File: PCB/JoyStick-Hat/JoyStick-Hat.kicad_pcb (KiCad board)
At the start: 2 copper layers, 73 parts, among them J1 Conn_02x10_Counter_Clockwise, J10 Conn_01x02_Pin, J11 Conn_01x02_Pin, J12 BU2032SM-JJ-GTR, J13 20021121-00010C4LF, J14 0675031020, J2 Conn_02x10_Counter_Clockwise, J3 Raspberry_Pi_2_3, J4 Conn_01x03_Pin, J5 Conn_01x03_Pin, J6 Conn_01x04_Pin, J7 Conn_01x02_Pin, J8 Conn_01x02_Pin, J9 Conn_01x04_Pin, M1 D24V22F12, M2 D24V22F5, M3 D24V22F3, SW1 TL3301NF260QG, U2 TLC5947DAP, U3 TLC5947DAP, U4 MAX3535ECWI+T, U5 STM32F446VETx, X1 ABM3B-8.000MHZ-B2-T, X2 ABS07-32.768KHZ-9-T

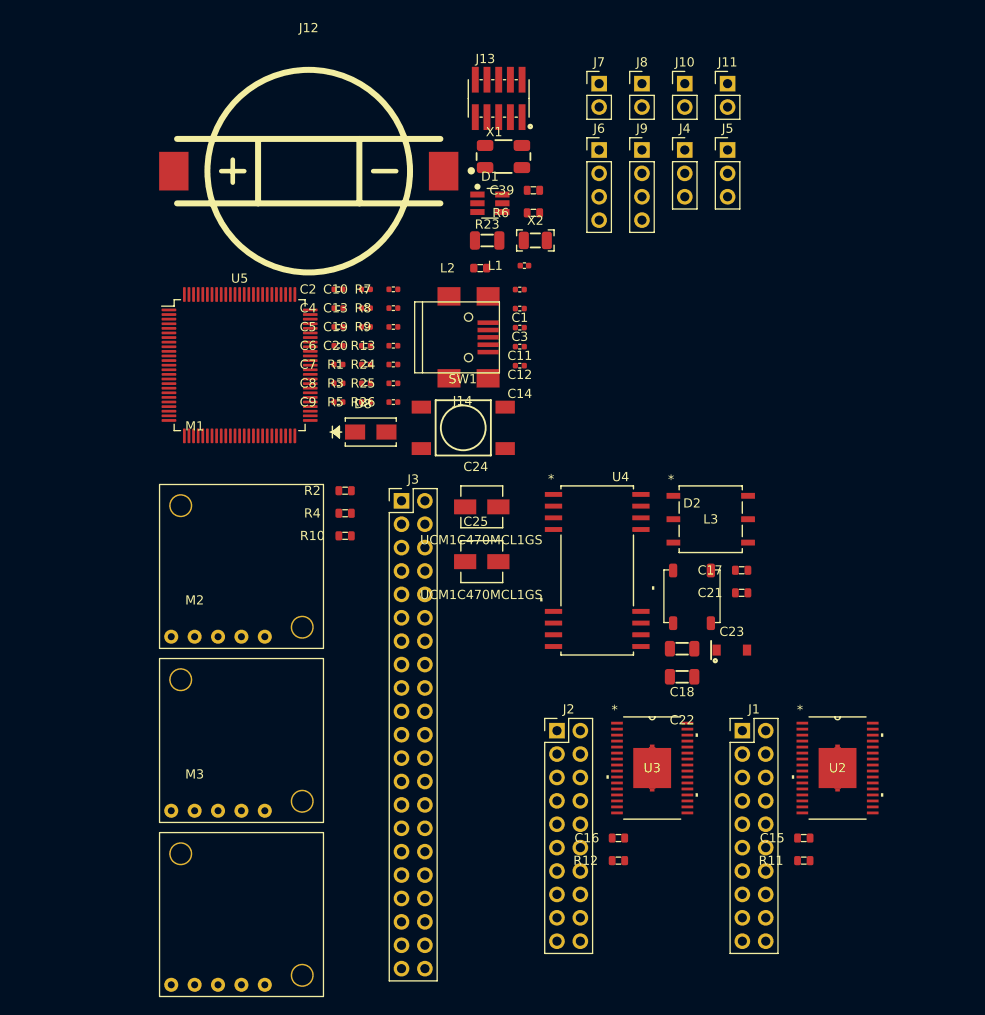
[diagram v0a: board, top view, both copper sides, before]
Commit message: LEDs and Additional connectors
Added heartbeat and diagnostic LEDs to STM32 and RPi3 schematics so we can directly flash them for debug purposes. Added a connector for serial port diagnostics on STM32. Added rotary switch interface for STM32 and added pullups to button connectors.
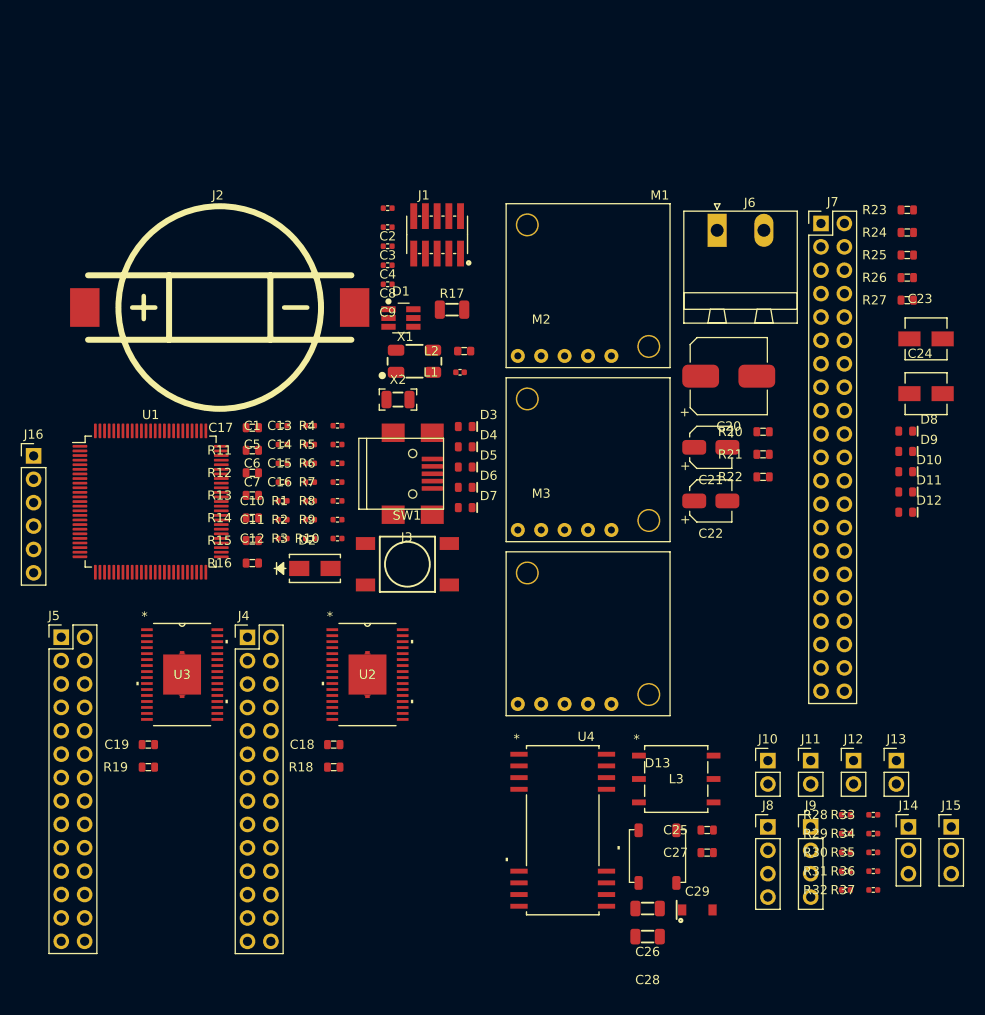
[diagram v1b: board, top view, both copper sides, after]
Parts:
- removed C39: C0603X103K1RAC3316, AVR-KiCAD-Lib-Capacitors:C0603
- removed U5: STM32F446VETx, Package_QFP:LQFP-100_14x14mm_P0.5mm
- added C26: CGA5L3X5R1V106K160AB, AVR-KiCAD-Lib-Capacitors:C1206, F.Cu at (155.7, 123.5)
- added C27: CL10B104JB8NNNC, AVR-KiCAD-Lib-Capacitors:C0603, F.Cu at (162.1, 117.4)
- added C28: CGA5L3X5R1V106K160AB, AVR-KiCAD-Lib-Capacitors:C1206, F.Cu at (155.7, 126.5)
- added C29: C1206C105K3RACAUTO, AVR-KiCAD-Lib-Diodes:D_SOD-123, F.Cu at (161.1, 123.6)
- added D10: LTST-C194KGKT, AVR-KiCAD-Lib-Diodes:LED0603, F.Cu at (183.7, 76.0)
- added D11: LTST-C194KGKT, AVR-KiCAD-Lib-Diodes:LED0603, F.Cu at (183.7, 78.2)
- added D12: LTST-C194KGKT, AVR-KiCAD-Lib-Diodes:LED0603, F.Cu at (183.7, 80.4)
- added D13: LMB110S-TP, AVR-KiCAD-Lib-Diodes:LMB110S-TP, F.Cu at (156.7, 117.8)
- added D3: LTST-C194TBKT, AVR-KiCAD-Lib-Diodes:LED0603, F.Cu at (135.9, 71.1)
- added D4: LTST-C194TBKT, AVR-KiCAD-Lib-Diodes:LED0603, F.Cu at (135.9, 73.3)
- added D5: LTST-C194TBKT, AVR-KiCAD-Lib-Diodes:LED0603, F.Cu at (135.9, 75.5)
- added D6: LTST-C194TBKT, AVR-KiCAD-Lib-Diodes:LED0603, F.Cu at (135.9, 77.7)
- added D7: LTST-C194TBKT, AVR-KiCAD-Lib-Diodes:LED0603, F.Cu at (135.9, 79.9)
- added D9: LTST-C194KGKT, AVR-KiCAD-Lib-Diodes:LED0603, F.Cu at (183.7, 73.8)
- added J15: Conn_01x03_Pin, Connector_PinHeader_2.54mm:PinHeader_1x03_P2.54mm_Vertical, F.Cu at (188.6, 114.6)
- added J16: Conn_01x06, Connector_PinHeader_2.54mm:PinHeader_1x06_P2.54mm_Vertical, F.Cu at (89.0, 74.3)
- added R14: RC0603FR-07470RL, AVR-KiCAD-Lib-Resistors:R0603, F.Cu at (112.8, 81.0)
- added R15: RC0603FR-07470RL, AVR-KiCAD-Lib-Resistors:R0603, F.Cu at (112.8, 83.5)
- added R16: RC0603FR-07470RL, AVR-KiCAD-Lib-Resistors:R0603, F.Cu at (112.8, 85.9)
- added R17: RC1206FR-071ML, AVR-KiCAD-Lib-Resistors:R1206, F.Cu at (134.4, 58.4)
- added R18: RMCF0603FT2K61, AVR-KiCAD-Lib-Resistors:R0603, F.Cu at (121.6, 108.1)
- added R19: RMCF0603FT2K61, AVR-KiCAD-Lib-Resistors:R0603, F.Cu at (101.5, 108.1)
- added R20: RC0603JR-07270RL, AVR-KiCAD-Lib-Resistors:R0603, F.Cu at (168.2, 71.7)
- added R21: RC0603JR-07270RL, AVR-KiCAD-Lib-Resistors:R0603, F.Cu at (168.2, 74.1)
- added R22: RC0603JR-07270RL, AVR-KiCAD-Lib-Resistors:R0603, F.Cu at (168.2, 76.6)
- added R27: RC0603FR-07470RL, AVR-KiCAD-Lib-Resistors:R0603, F.Cu at (183.9, 57.4)
- added R28: RC0402FR-071KL, AVR-KiCAD-Lib-Resistors:R0402, F.Cu at (177.2, 113.3)
- added R29: RC0402FR-071KL, AVR-KiCAD-Lib-Resistors:R0402, F.Cu at (177.2, 115.3)
- added R30: RC0402FR-071KL, AVR-KiCAD-Lib-Resistors:R0402, F.Cu at (177.2, 117.4)
- added R31: RC0402FR-071KL, AVR-KiCAD-Lib-Resistors:R0402, F.Cu at (177.2, 119.4)
- added R32: RC0402FR-071KL, AVR-KiCAD-Lib-Resistors:R0402, F.Cu at (177.2, 121.4)
- added R33: RC0402FR-071KL, AVR-KiCAD-Lib-Resistors:R0402, F.Cu at (180.2, 113.3)
- added R34: RC0402FR-071KL, AVR-KiCAD-Lib-Resistors:R0402, F.Cu at (180.2, 115.3)
- added R35: RC0402FR-071KL, AVR-KiCAD-Lib-Resistors:R0402, F.Cu at (180.2, 117.4)
- added R36: RC0402FR-071KL, AVR-KiCAD-Lib-Resistors:R0402, F.Cu at (180.2, 119.4)
- added R37: RC0402FR-071KL, AVR-KiCAD-Lib-Resistors:R0402, F.Cu at (180.2, 121.4)
- added U1: STM32F446VETx, Package_QFP:LQFP-100_14x14mm_P0.5mm, F.Cu at (101.7, 79.3)
- C1: value GCM1555C1H180GA16D -> C0402C104K9PACTU; footprint AVR-KiCAD-Lib-Capacitors:C0402 -> AVR-KiCAD-Lib-Resistors:R0402
- C11, C12: value CL05C090CB5NNNC -> C0402C104K9PACTU; footprint AVR-KiCAD-Lib-Capacitors:C0402 -> AVR-KiCAD-Lib-Resistors:R0402
- C14: value GRM155R60J475ME47D -> C0402C104K9PACTU; footprint AVR-KiCAD-Lib-Capacitors:C0402 -> AVR-KiCAD-Lib-Resistors:R0402
- C15, C16: value CL10B104JB8NNNC -> C0402C104K9PACTU; footprint AVR-KiCAD-Lib-Capacitors:C0603 -> AVR-KiCAD-Lib-Resistors:R0402
- C17: value CL10B104JB8NNNC -> C0603X103K1RAC3316
- C18: value CGA5L3X5R1V106K160AB -> CL10B104JB8NNNC; footprint AVR-KiCAD-Lib-Capacitors:C1206 -> AVR-KiCAD-Lib-Capacitors:C0603
- C19: value C0402C104K9PACTU -> CL10B104JB8NNNC; footprint AVR-KiCAD-Lib-Resistors:R0402 -> AVR-KiCAD-Lib-Capacitors:C0603
- C2, C4: value C0402C104K9PACTU -> GCM1555C1H180GA16D; footprint AVR-KiCAD-Lib-Resistors:R0402 -> AVR-KiCAD-Lib-Capacitors:C0402
- C20: value C0402C104K9PACTU -> UUQ1H470MCL1GS; footprint AVR-KiCAD-Lib-Resistors:R0402 -> AVR-KiCAD-Lib-Capacitors:CP_Elec_8x10
- C21: value CL10B104JB8NNNC -> UUQ1H100MCL1GB; footprint AVR-KiCAD-Lib-Capacitors:C0603 -> AVR-KiCAD-Lib-Capacitors:CP_Elec_4x5.3
- C22: value CGA5L3X5R1V106K160AB -> UUQ1H010MCL1GB; footprint AVR-KiCAD-Lib-Capacitors:C1206 -> AVR-KiCAD-Lib-Capacitors:CP_Elec_4x5.3
- C23: value C1206C105K3RACAUTO -> UCM1C470MCL1GS; footprint AVR-KiCAD-Lib-Diodes:D_SOD-123 -> AVR-KiCAD-Lib-Capacitors:UCM1C470MCL1GS
- C25: value UCM1C470MCL1GS -> CL10B104JB8NNNC; footprint AVR-KiCAD-Lib-Capacitors:UCM1C470MCL1GS -> AVR-KiCAD-Lib-Capacitors:C0603
- C3: value GCM1555C1H180GA16D -> GRM155R60J475ME47D
- C8, C9: value C0402C104K9PACTU -> CL05C090CB5NNNC; footprint AVR-KiCAD-Lib-Resistors:R0402 -> AVR-KiCAD-Lib-Capacitors:C0402
- D2: value LMB110S-TP -> SMAJ30CA; footprint AVR-KiCAD-Lib-Diodes:LMB110S-TP -> AVR-KiCAD-Lib-Diodes:SMAJ30CA
- D8: value SMAJ30CA -> LTST-C194KGKT; footprint AVR-KiCAD-Lib-Diodes:SMAJ30CA -> AVR-KiCAD-Lib-Diodes:LED0603
- J1: value Conn_02x10_Counter_Clockwise -> 20021121-00010C4LF; footprint Connector_PinHeader_2.54mm:PinHeader_2x10_P2.54mm_Vertical -> AVR-KiCAD-Lib-Connectors:20021121-00010C4LF
- J12: value BU2032SM-JJ-GTR -> Conn_01x02_Pin; footprint AVR-KiCAD-Lib-Battery-Holders:BU2032SM-JJ-GTR -> Connector_PinHeader_2.54mm:PinHeader_1x02_P2.54mm_Vertical
- J13: value 20021121-00010C4LF -> Conn_01x02_Pin; footprint AVR-KiCAD-Lib-Connectors:20021121-00010C4LF -> Connector_PinHeader_2.54mm:PinHeader_1x02_P2.54mm_Vertical
- J14: value 0675031020 -> Conn_01x03_Pin; footprint AVR-KiCAD-Lib-Connectors:USB_Mini-B -> Connector_PinHeader_2.54mm:PinHeader_1x03_P2.54mm_Vertical
- J2: value Conn_02x10_Counter_Clockwise -> BU2032SM-JJ-GTR; footprint Connector_PinHeader_2.54mm:PinHeader_2x10_P2.54mm_Vertical -> AVR-KiCAD-Lib-Battery-Holders:BU2032SM-JJ-GTR
- J3: value Raspberry_Pi_2_3 -> 0675031020; footprint Connector_PinHeader_2.54mm:PinHeader_2x21_P2.54mm_Vertical -> AVR-KiCAD-Lib-Connectors:USB_Mini-B
- J4, J5: value Conn_01x03_Pin -> Conn_02x14_Counter_Clockwise; footprint Connector_PinHeader_2.54mm:PinHeader_1x03_P2.54mm_Vertical -> Connector_PinHeader_2.54mm:PinHeader_2x14_P2.54mm_Vertical
- J6: value Conn_01x04_Pin -> 1757242; footprint Connector_PinHeader_2.54mm:PinHeader_1x04_P2.54mm_Vertical -> AVR-KiCAD-Lib-Connectors:PhoenixContact_MSTBA-G_02x5.08mm_Angled
- J7: value Conn_01x02_Pin -> Raspberry_Pi_2_3; footprint Connector_PinHeader_2.54mm:PinHeader_1x02_P2.54mm_Vertical -> Connector_PinHeader_2.54mm:PinHeader_2x21_P2.54mm_Vertical
- J8: value Conn_01x02_Pin -> Conn_01x04_Pin; footprint Connector_PinHeader_2.54mm:PinHeader_1x02_P2.54mm_Vertical -> Connector_PinHeader_2.54mm:PinHeader_1x04_P2.54mm_Vertical
- R10: value RC0603JR-07270RL -> RC0402FR-0710KL; footprint AVR-KiCAD-Lib-Resistors:R0603 -> AVR-KiCAD-Lib-Resistors:R0402
- R11: value RMCF0603FT2K61 -> RC0603FR-0747KL
- R12: value RMCF0603FT2K61 -> RC0603FR-07470RL
- R13, R25: value RC0402FR-0710KL -> RC0603FR-07470RL; footprint AVR-KiCAD-Lib-Resistors:R0402 -> AVR-KiCAD-Lib-Resistors:R0603
- R2, R4: value RC0603JR-07270RL -> RC0402FR-071KL; footprint AVR-KiCAD-Lib-Resistors:R0603 -> AVR-KiCAD-Lib-Resistors:R0402
- R23: value RC1206FR-071ML -> RC0603FR-07470RL; footprint AVR-KiCAD-Lib-Resistors:R1206 -> AVR-KiCAD-Lib-Resistors:R0603
- R24, R26: value RC0402FR-0722RL -> RC0603FR-07470RL; footprint AVR-KiCAD-Lib-Resistors:R0402 -> AVR-KiCAD-Lib-Resistors:R0603
- R5: value RC0402FR-071KL -> RC0402FR-0710KL
- R6: value RC0603FR-0747KL -> RC0402FR-071KL; footprint AVR-KiCAD-Lib-Resistors:R0603 -> AVR-KiCAD-Lib-Resistors:R0402
- R8, R9: value RC0402FR-071KL -> RC0402FR-0722RL
- moved J5 89.6 mm to (92.0, 94.0)
- moved J12 87.2 mm to (178.0, 107.4)
- moved J13 83.9 mm to (182.7, 107.4)
- moved J8 81.9 mm to (168.7, 114.6)
- moved J9 75.8 mm to (173.4, 114.6)
- moved R11 74.6 mm to (112.8, 73.7)
- moved J10 74.1 mm to (168.7, 107.4)
- moved J11 74.1 mm to (173.4, 107.4)
- moved J14 71.5 mm to (184.0, 114.6)
- moved J4 71.1 mm to (112.2, 94.0)
- moved C15 67.3 mm to (119.0, 75.1)
- moved J1 63.2 mm to (132.8, 50.3)
- moved J2 58.8 mm to (109.2, 58.2)
- moved D8 58.1 mm to (183.7, 71.6)
- moved R12 57.9 mm to (112.8, 76.1)
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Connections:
- C1 pad 1: /STM32F446RET6-MCU/OSC_IN -> /STM32F446RET6-MCU/VCAP1
- C10 pad 1: /STM32F446RET6-MCU/NRST -> +3V3
- C11 pad 1: GND -> Net-(C11-Pad1)
- C11 pad 2: /STM32F446RET6-MCU/OSC32_OUT -> GND
- C12 pad 1: GND -> Net-(C11-Pad1)
- C12 pad 2: /STM32F446RET6-MCU/OSC32_IN -> GND
- C13 pad 1: /STM32F446RET6-MCU/VCAP1 -> Net-(C11-Pad1)
- C14 pad 1: /STM32F446RET6-MCU/VCAP1 -> Net-(C11-Pad1)
- C15 pad 1: GND -> Net-(C11-Pad1)
- C15 pad 2: +3.3V -> GND
- C16 pad 1: GND -> Net-(C11-Pad1)
- C16 pad 2: +3.3V -> GND
- C17 pad 2: +3.3V -> Net-(J3-SHL)
- C19 pad 1: Net-(C19-Pad1) -> GND
- C19 pad 2: GND -> +3.3V
- C2 pad 1: +3V3 -> /STM32F446RET6-MCU/OSC_IN
- C20 pad 1: Net-(C19-Pad1) -> +24V
- C21 pad 1: Earth -> +24V
- C21 pad 2: +5V -> GND
- C22 pad 1: Earth -> +24V
- C22 pad 2: +5V -> GND
- C23 pad 1: Earth -> +5V
- C23 pad 2: +5V -> GND
- C25 pad 1: +5V -> GND
- C25 pad 2: GND -> +3.3V
- C3 pad 1: /STM32F446RET6-MCU/OSC_OUT -> /STM32F446RET6-MCU/VCAP1
- C4 pad 1: /STM32F446RET6-MCU/VBAT -> /STM32F446RET6-MCU/OSC_OUT
- C5 pad 1: /STM32F446RET6-MCU/VDDA -> /STM32F446RET6-MCU/NRST
- C6 pad 1: Net-(C19-Pad1) -> /STM32F446RET6-MCU/VBAT
- C7 pad 1: Net-(C19-Pad1) -> /STM32F446RET6-MCU/VDDA
- C8 pad 1: Net-(C19-Pad1) -> GND
- C8 pad 2: GND -> /STM32F446RET6-MCU/OSC32_OUT
- C9 pad 1: Net-(C19-Pad1) -> GND
- C9 pad 2: GND -> /STM32F446RET6-MCU/OSC32_IN
- D1 pad 6: Net-(J14-ID) -> Net-(J3-ID)
- D2 pad 1: Net-(D2-Pad1) -> Net-(J3-SHL)
- D2 pad 2: Net-(D2-Pad2) -> GND
- D8 pad 1: Net-(J14-SHL) -> Net-(D8-Pad1)
- J1 pad 1: Net-(J1-Pin_1) -> +3V3
- J1 pad 10: Net-(J1-Pin_10) -> /STM32F446RET6-MCU/NJTRST
- J1 pad 2: Net-(J1-Pin_2) -> /STM32F446RET6-MCU/SWDIO_TMS
- J1 pad 3: Net-(J1-Pin_3) -> GND
- J1 pad 4: Net-(J1-Pin_4) -> /STM32F446RET6-MCU/SWCLK_TCK
- J1 pad 5: Net-(J1-Pin_5) -> GND
- J1 pad 6: Net-(J1-Pin_6) -> /STM32F446RET6-MCU/SWO_TDO
- J1 pad 7: Net-(J1-Pin_7) -> unconnected-(J1-Pad7)
- J1 pad 8: Net-(J1-Pin_8) -> /STM32F446RET6-MCU/SWO_TDI
- J1 pad 9: Net-(J1-Pin_9) -> GND
- J10 pad 1: /JoyStick Interface/BUTTON3 -> /JoyStick Interface/BUTTON1
- J11 pad 1: /JoyStick Interface/BUTTON4 -> /JoyStick Interface/BUTTON2
- J12 pad 1: /STM32F446RET6-MCU/VBAT -> /JoyStick Interface/BUTTON3
- J12 pad 2: GND -> unconnected-(J12-Pin_2-Pad2)
- J13 pad 1: +3V3 -> /JoyStick Interface/BUTTON4
- J13 pad 2: /STM32F446RET6-MCU/SWDIO_TMS -> unconnected-(J13-Pin_2-Pad2)
- J14 pad 1: /STM32F446RET6-MCU/VBUS -> GND
- J14 pad 2: /STM32F446RET6-MCU/D- -> /JoyStick Interface/JOYSTICK_X
- J14 pad 3: /STM32F446RET6-MCU/D+ -> +3.3V
- J2 pad 1: Net-(J2-Pin_1) -> /STM32F446RET6-MCU/VBAT
- J2 pad 2: Net-(J2-Pin_2) -> GND
- J3 pad 1: unconnected-(J3-3V3-Pad1) -> /STM32F446RET6-MCU/VBUS
- J3 pad 2: +5V -> /STM32F446RET6-MCU/D-
- J3 pad 3: unconnected-(J3-SDA/GPIO2-Pad3) -> /STM32F446RET6-MCU/D+
- J3 pad 4: +5V -> Net-(J3-ID)
- J3 pad 5: unconnected-(J3-SCL/GPIO3-Pad5) -> GND
- J3 pad 6: GND -> Net-(J3-SHL)
- J4 pad 2: /JoyStick Interface/JOYSTICK_Y -> GND
- J4 pad 3: +3.3V -> Net-(J4-Pin_3)
- J5 pad 2: /JoyStick Interface/JOYSTICK_X -> GND
- J5 pad 3: +3.3V -> Net-(J5-Pin_3)
- J6 pad 1: unconnected-(J6-Pin_1-Pad1) -> +24V
- J6 pad 2: unconnected-(J6-Pin_2-Pad2) -> GND
- J7 pad 1: /JoyStick Interface/BUTTON1 -> unconnected-(J7-3V3-Pad1)
- J7 pad 2: unconnected-(J7-Pin_2-Pad2) -> +5V
- J8 pad 1: /JoyStick Interface/BUTTON2 -> /JoyStick Interface/ROTARY1_POLE1
- J8 pad 2: unconnected-(J8-Pin_2-Pad2) -> /JoyStick Interface/ROTARY1_POLE2
- J9 pad 1: unconnected-(J9-Pin_1-Pad1) -> /JoyStick Interface/ROTARY2_POLE1
- J9 pad 2: unconnected-(J9-Pin_2-Pad2) -> /JoyStick Interface/ROTARY2_POLE2
- J9 pad 3: unconnected-(J9-Pin_3-Pad3) -> /JoyStick Interface/ROTARY2_POLE3
- J9 pad 4: unconnected-(J9-Pin_4-Pad4) -> GND
- L2 pad 1: Net-(J14-SHL) -> Net-(J3-SHL)
- L3 pad 4: Net-(D2-Pad2) -> Net-(D13-Pad2)
- L3 pad 6: Net-(D2-Pad1) -> Net-(D13-Pad1)
- R10 pad 1: /Power/3.3V_PG -> /STM32F446RET6-MCU/MCU_VBUS
- R10 pad 2: +3.3V -> /STM32F446RET6-MCU/VBUS
- R11 pad 1: GND -> Net-(J3-ID)
- R11 pad 2: Net-(U2-IREF) -> GND
- R12 pad 1: GND -> Net-(U1-PB5)
- R12 pad 2: Net-(U3-IREF) -> Net-(D3-Pad1)
- R13 pad 1: GND -> Net-(U1-PB6)
- R2 pad 1: /Power/12V_PG -> +3V3
- R2 pad 2: +3.3V -> /STM32F446RET6-MCU/SWDIO_TMS
- R23 pad 1: Net-(J14-SHL) -> Net-(D8-Pad1)
- R23 pad 2: GND -> Net-(J7-GPIO22)
- R24 pad 1: /STM32F446RET6-MCU/MCU_D- -> Net-(D9-Pad1)
- R24 pad 2: /STM32F446RET6-MCU/D- -> Net-(J7-GPIO23)
- R25 pad 1: /STM32F446RET6-MCU/MCU_VBUS -> Net-(D10-Pad1)
- R25 pad 2: /STM32F446RET6-MCU/VBUS -> Net-(J7-GPIO24)
- R26 pad 1: /STM32F446RET6-MCU/MCU_D+ -> Net-(D11-Pad1)
- R26 pad 2: /STM32F446RET6-MCU/D+ -> Net-(J7-GPIO25)
- R3 pad 2: /STM32F446RET6-MCU/SWDIO_TMS -> /STM32F446RET6-MCU/SWCLK_TCK
- R4 pad 1: /Power/5V_PG -> +3V3
- R4 pad 2: +3.3V -> /STM32F446RET6-MCU/SWO_TDO
- R5 pad 1: +3V3 -> GND
- R5 pad 2: /STM32F446RET6-MCU/SWCLK_TCK -> Net-(U1-BOOT0)
- R6 pad 1: Net-(J14-ID) -> +3V3
- R6 pad 2: GND -> /STM32F446RET6-MCU/SWO_TDI
- R7 pad 2: /STM32F446RET6-MCU/SWO_TDO -> /STM32F446RET6-MCU/NJTRST
- R8 pad 1: +3V3 -> /STM32F446RET6-MCU/MCU_D-
- R8 pad 2: /STM32F446RET6-MCU/SWO_TDI -> /STM32F446RET6-MCU/D-
- R9 pad 1: +3V3 -> /STM32F446RET6-MCU/MCU_D+
- R9 pad 2: /STM32F446RET6-MCU/NJTRST -> /STM32F446RET6-MCU/D+
- U2 pad 10: Net-(J1-Pin_6) -> Net-(J4-Pin_8)
- U2 pad 11: Net-(J1-Pin_7) -> Net-(J4-Pin_9)
- U2 pad 12: Net-(J1-Pin_8) -> Net-(J4-Pin_10)
- U2 pad 13: Net-(J1-Pin_9) -> Net-(J4-Pin_11)
- U2 pad 14: Net-(J1-Pin_10) -> Net-(J4-Pin_12)
- U2 pad 15: Net-(J1-Pin_11) -> Net-(J4-Pin_13)
- U2 pad 16: Net-(J1-Pin_12) -> Net-(J4-Pin_14)
- U2 pad 17: Net-(J1-Pin_13) -> Net-(J4-Pin_15)
- U2 pad 18: Net-(J1-Pin_14) -> Net-(J4-Pin_16)
- U2 pad 19: Net-(J1-Pin_15) -> Net-(J4-Pin_17)
- U2 pad 20: Net-(J1-Pin_16) -> Net-(J4-Pin_18)
- U2 pad 21: Net-(J1-Pin_17) -> Net-(J4-Pin_19)
- U2 pad 22: Net-(J1-Pin_18) -> Net-(J4-Pin_20)
- U2 pad 23: Net-(J1-Pin_19) -> Net-(J4-Pin_21)
- U2 pad 24: Net-(J1-Pin_20) -> Net-(J4-Pin_22)
- U2 pad 25: unconnected-(U2-OUT20-Pad25) -> Net-(J4-Pin_23)
- U2 pad 26: unconnected-(U2-OUT21-Pad26) -> Net-(J4-Pin_24)
- U2 pad 27: unconnected-(U2-OUT22-Pad27) -> Net-(J4-Pin_25)
- U2 pad 28: unconnected-(U2-OUT23-Pad28) -> Net-(J4-Pin_26)
- U2 pad 5: Net-(J1-Pin_1) -> Net-(J4-Pin_3)
- U2 pad 6: Net-(J1-Pin_2) -> Net-(J4-Pin_4)
- U2 pad 7: Net-(J1-Pin_3) -> Net-(J4-Pin_5)
- U2 pad 8: Net-(J1-Pin_4) -> Net-(J4-Pin_6)
- U2 pad 9: Net-(J1-Pin_5) -> Net-(J4-Pin_7)
- U3 pad 10: Net-(J2-Pin_6) -> Net-(J5-Pin_8)
- U3 pad 11: Net-(J2-Pin_7) -> Net-(J5-Pin_9)
- U3 pad 12: Net-(J2-Pin_8) -> Net-(J5-Pin_10)
- U3 pad 13: Net-(J2-Pin_9) -> Net-(J5-Pin_11)
- U3 pad 14: Net-(J2-Pin_10) -> Net-(J5-Pin_12)
- U3 pad 15: Net-(J2-Pin_11) -> Net-(J5-Pin_13)
- U3 pad 16: Net-(J2-Pin_12) -> Net-(J5-Pin_14)
- U3 pad 17: Net-(J2-Pin_13) -> Net-(J5-Pin_15)
- U3 pad 18: Net-(J2-Pin_14) -> Net-(J5-Pin_16)
- U3 pad 19: Net-(J2-Pin_15) -> Net-(J5-Pin_17)
- U3 pad 20: Net-(J2-Pin_16) -> Net-(J5-Pin_18)
- U3 pad 21: Net-(J2-Pin_17) -> Net-(J5-Pin_19)
- U3 pad 22: Net-(J2-Pin_18) -> Net-(J5-Pin_20)
- U3 pad 23: Net-(J2-Pin_19) -> Net-(J5-Pin_21)
- U3 pad 24: Net-(J2-Pin_20) -> Net-(J5-Pin_22)
- U3 pad 25: unconnected-(U3-OUT20-Pad25) -> Net-(J5-Pin_23)
- U3 pad 26: unconnected-(U3-OUT21-Pad26) -> Net-(J5-Pin_24)
- U3 pad 27: unconnected-(U3-OUT22-Pad27) -> Net-(J5-Pin_25)
- U3 pad 28: unconnected-(U3-OUT23-Pad28) -> Net-(J5-Pin_26)
- U3 pad 5: Net-(J2-Pin_1) -> Net-(J5-Pin_3)
- U3 pad 6: Net-(J2-Pin_2) -> Net-(J5-Pin_4)
- U3 pad 7: Net-(J2-Pin_3) -> Net-(J5-Pin_5)
- U3 pad 8: Net-(J2-Pin_4) -> Net-(J5-Pin_6)
- U3 pad 9: Net-(J2-Pin_5) -> Net-(J5-Pin_7)

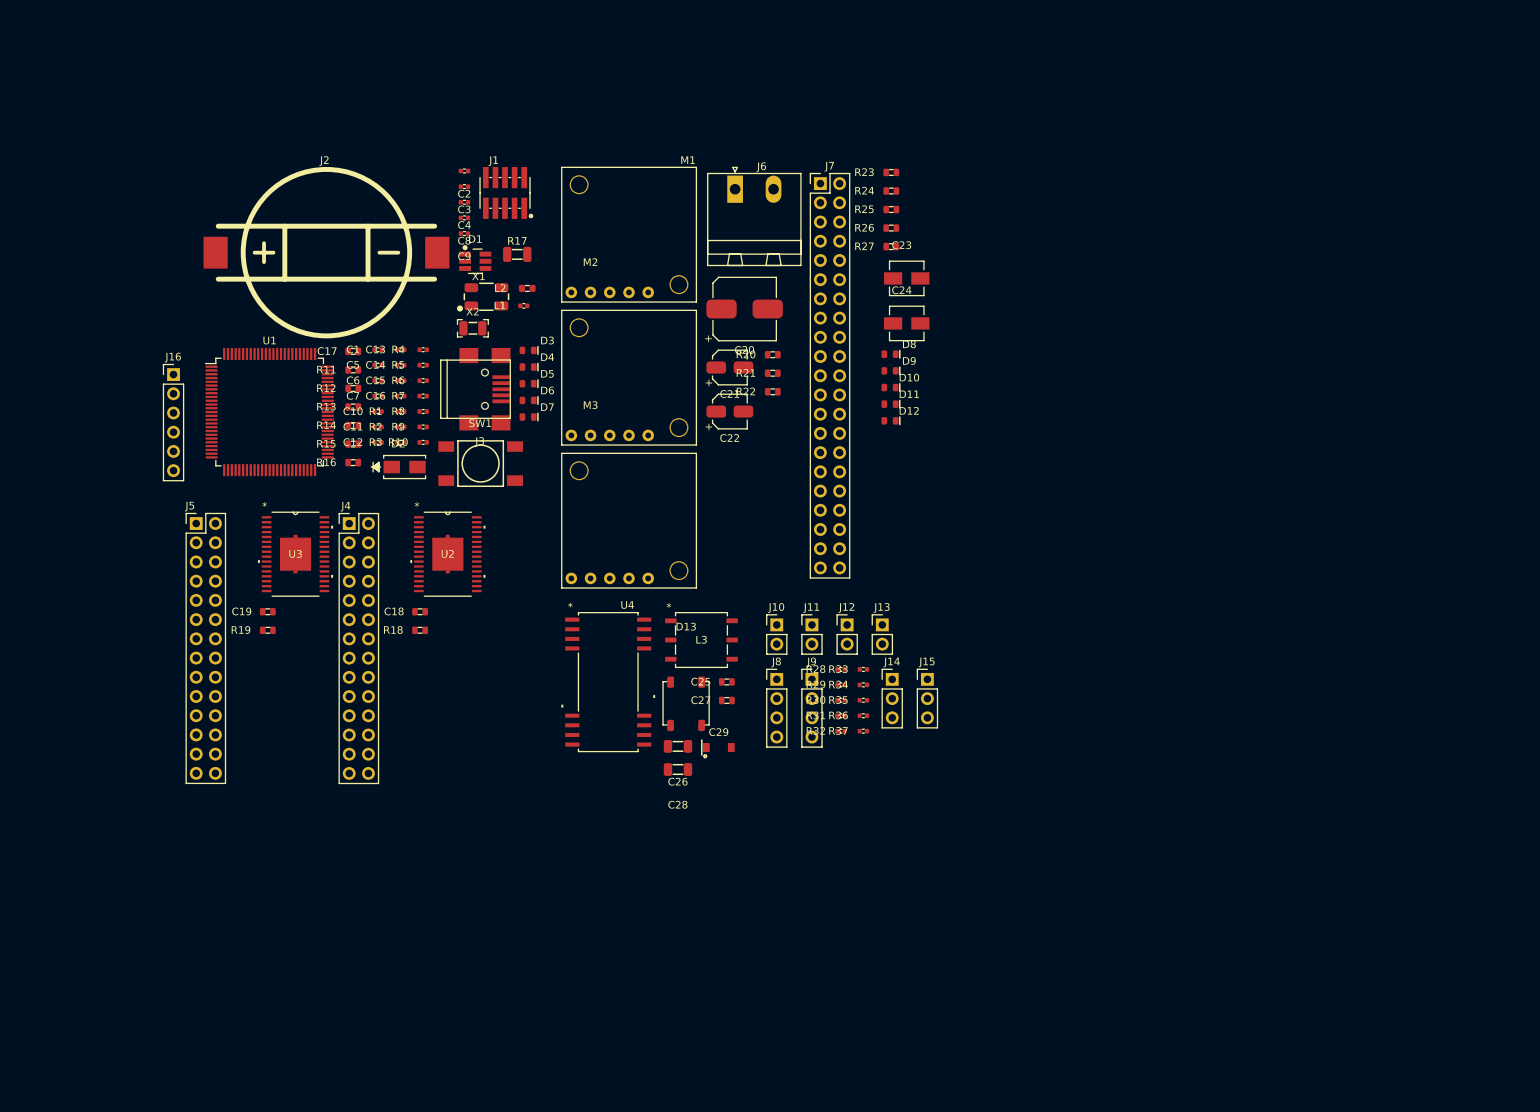
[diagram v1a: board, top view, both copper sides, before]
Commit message: Board Shape and Layout
Board Shape added and layout started !
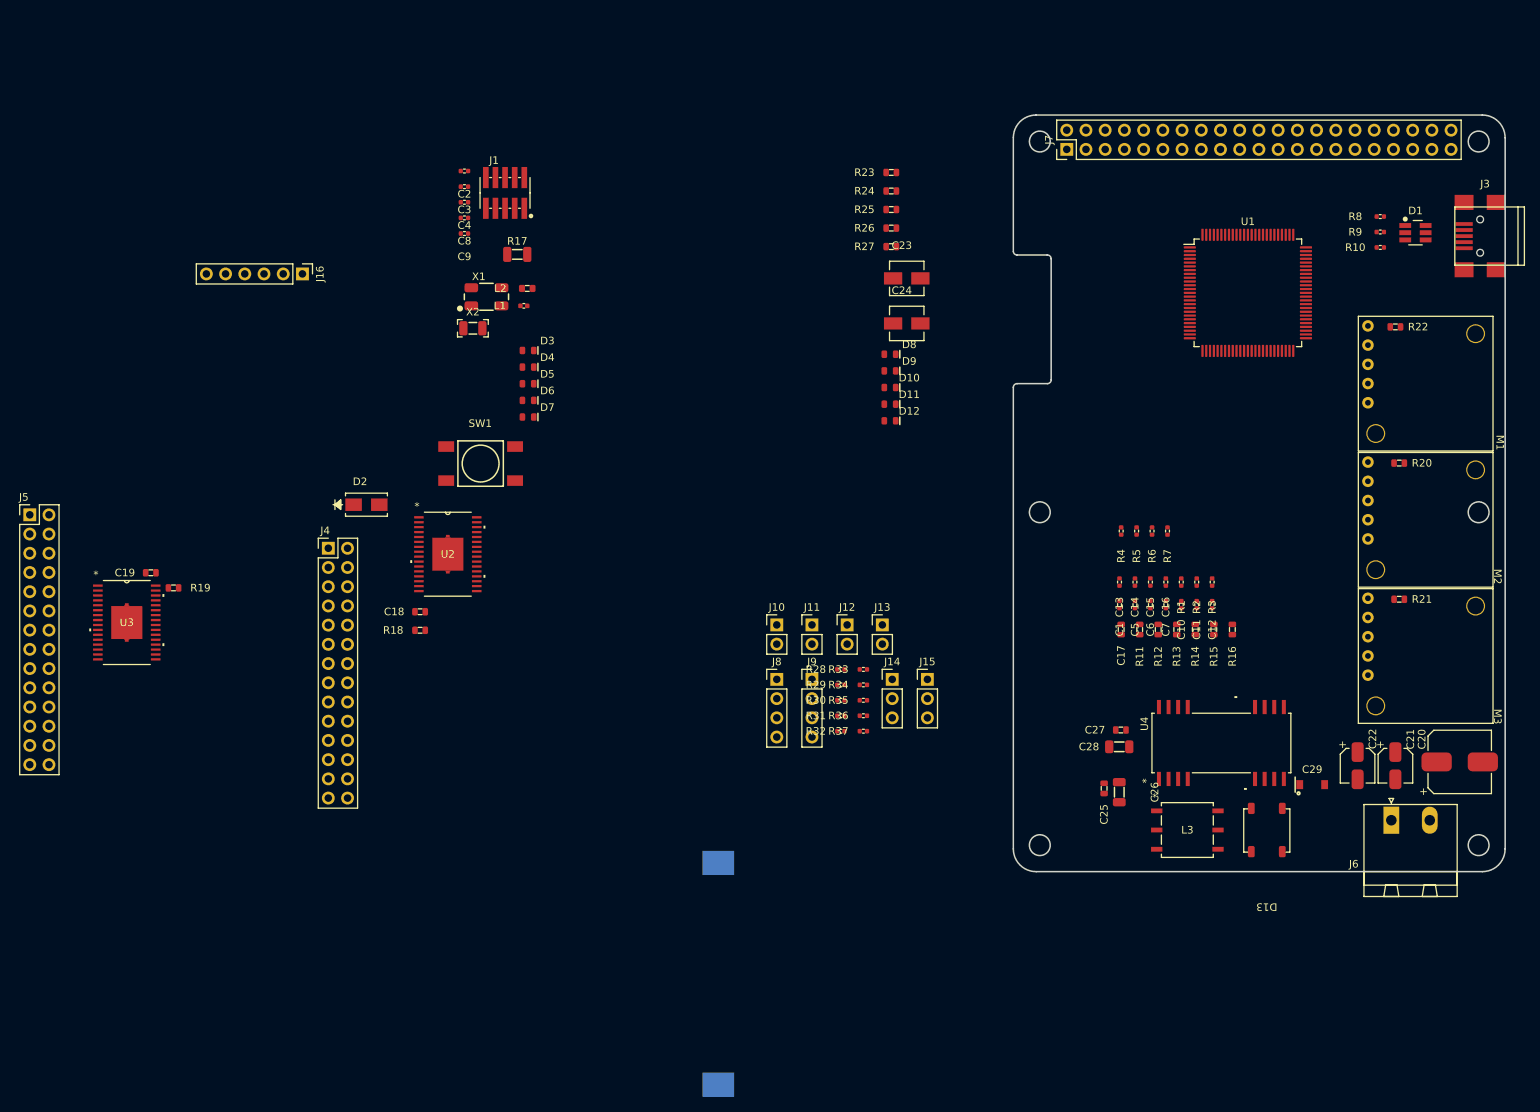
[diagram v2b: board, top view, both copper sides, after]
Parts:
- J2: moved to B.Cu
- moved J3 133.1 mm to (261.7, 56.0), turned to 180 degrees
- moved U1 130.3 mm to (231.0, 63.5)
- moved R10 129.1 mm to (248.5, 57.5)
- moved R8 129.1 mm to (248.5, 53.4)
- moved R9 129.1 mm to (248.5, 55.5)
- moved D1 124.3 mm to (253.2, 55.5)
- moved J6 120.3 mm to (250.0, 133.2)
- moved R16 118.3 mm to (228.9, 108.0), turned to 90 degrees
- moved R15 116.4 mm to (226.5, 108.0), turned to 90 degrees
- moved R14 114.5 mm to (224.1, 108.0), turned to 90 degrees
- moved R13 112.8 mm to (221.6, 108.0), turned to 90 degrees
- moved C12 112.3 mm to (226.3, 104.7), turned to 90 degrees
- moved C20 111.9 mm to (259.0, 125.5)
- moved R12 111.1 mm to (219.2, 108.0), turned to 90 degrees
- moved C11 110.7 mm to (224.2, 104.7), turned to 90 degrees
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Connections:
- J14 pad 2: /JoyStick Interface/JOYSTICK_X -> +3.3V
- J14 pad 3: +3.3V -> /JoyStick Interface/JOYSTICK_X
- J15 pad 2: /JoyStick Interface/JOYSTICK_Y -> +3.3V
- J15 pad 3: +3.3V -> /JoyStick Interface/JOYSTICK_Y
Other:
- board outline added: 65 x 100 mm
